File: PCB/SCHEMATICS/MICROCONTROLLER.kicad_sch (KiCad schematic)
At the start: 29 parts, among them IC1 CP2102-GMR, U6 C6482, U7 C6482

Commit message: updated path for footprints
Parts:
- C6: footprint 0ohm:RESC1005X40N -> footprint:RESC1005X40N
- R25, R27: footprint 2.2k:RESC1005X40N -> footprint:RESC1005X40N
- TP22, TP23, TP24, TP25, TP26, TP27, TP32, TP33, TP34, TP35: footprint TestPoint:TestPoint_Bridge_Pitch2.0mm_Drill0.7mm -> TestPoint:TestPoint_Pad_D2.0mm
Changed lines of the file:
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@@
       (effects (font (size 1.27 1.27)))
     )
-    (property "Footprint" "0ohm:RESC1005X40N" (at 127.635 127.635 0)
+    (property "Footprint" "footprint:RESC1005X40N" (at 127.635 127.635 0)
       (effects (font (size 1.27 1.27)) hide)
     )
@@
       (effects (font (size 1.27 1.27)))
     )
-    (property "Footprint" "0ohm:RESC1005X40N" (at 203.2 53.34 0)
+    (property "Footprint" "footprint:RESC1005X40N" (at 203.2 53.34 0)
       (effects (font (size 1.27 1.27)) hide)
     )
@@
       (effects (font (size 1.27 1.27)) (justify right))
     )
-    (property "Footprint" "0ohm:RESC1005X40N" (at 41.91 95.504 0)
+    (property "Footprint" "footprint:RESC1005X40N" (at 41.91 95.504 0)
       (effects (font (size 1.27 1.27)) hide)
     )
@@
       (effects (font (size 1.27 1.27)) (justify left))
     )
-    (property "Footprint" "TestPoint:TestPoint_Bridge_Pitch2.0mm_Drill0.7mm" (at 158.75 39.37 0)
+    (property "Footprint" "TestPoint:TestPoint_Pad_D2.0mm" (at 158.75 39.37 0)
       (effects (font (size 1.27 1.27)) hide)
     )
@@
       (effects (font (size 1.27 1.27)))
     )
-    (property "Footprint" "0ohm:RESC1005X40N" (at 76.2 124.46 0)
+    (property "Footprint" "footprint:RESC1005X40N" (at 76.2 124.46 0)
       (effects (font (size 1.27 1.27)) hide)
     )
@@
       (effects (font (size 1.27 1.27)))
     )
-    (property "Footprint" "2.2k:RESC1005X40N" (at 185.42 53.34 0)
+    (property "Footprint" "footprint:RESC1005X40N" (at 185.42 53.34 0)
       (effects (font (size 1.27 1.27)) hide)
     )
@@
       (effects (font (size 1.27 1.27)))
     )
-    (property "Footprint" "0ohm:RESC1005X40N" (at 127.635 107.315 0)
+    (property "Footprint" "footprint:RESC1005X40N" (at 127.635 107.315 0)
       (effects (font (size 1.27 1.27)) hide)
     )
@@
       (effects (font (size 1.27 1.27)))
     )
-    (property "Footprint" "0ohm:RESC1005X40N" (at 76.2 121.92 0)
+    (property "Footprint" "footprint:RESC1005X40N" (at 76.2 121.92 0)
       (effects (font (size 1.27 1.27)) hide)
     )
@@
       (effects (font (size 1.27 1.27)) (justify left))
     )
-    (property "Footprint" "TestPoint:TestPoint_Bridge_Pitch2.0mm_Drill0.7mm" (at 140.97 39.37 0)
+    (property "Footprint" "TestPoint:TestPoint_Pad_D2.0mm" (at 140.97 39.37 0)
       (effects (font (size 1.27 1.27)) hide)
     )
@@
       (effects (font (size 1.27 1.27)) (justify left))
     )
-    (property "Footprint" "TestPoint:TestPoint_Bridge_Pitch2.0mm_Drill0.7mm" (at 52.07 168.91 0)
+    (property "Footprint" "TestPoint:TestPoint_Pad_D2.0mm" (at 52.07 168.91 0)
       (effects (font (size 1.27 1.27)) hide)
     )
@@
       (effects (font (size 1.27 1.27)))
     )
-    (property "Footprint" "2.2k:RESC1005X40N" (at 185.42 50.8 0)
+    (property "Footprint" "footprint:RESC1005X40N" (at 185.42 50.8 0)
       (effects (font (size 1.27 1.27)) hide)
     )
@@
       (effects (font (size 1.27 1.27)))
     )
-    (property "Footprint" "0ohm:RESC1005X40N" (at 203.2 50.8 0)
+    (property "Footprint" "footprint:RESC1005X40N" (at 203.2 50.8 0)
       (effects (font (size 1.27 1.27)) hide)
     )
@@
       (effects (font (size 1.27 1.27)) (justify left))
     )
-    (property "Footprint" "TestPoint:TestPoint_Bridge_Pitch2.0mm_Drill0.7mm" (at 52.07 171.45 0)
+    (property "Footprint" "TestPoint:TestPoint_Pad_D2.0mm" (at 52.07 171.45 0)
       (effects (font (size 1.27 1.27)) hide)
     )
@@
       (effects (font (size 1.27 1.27)) (justify left))
     )
-    (property "Footprint" "TestPoint:TestPoint_Bridge_Pitch2.0mm_Drill0.7mm" (at 175.26 39.37 0)
+    (property "Footprint" "TestPoint:TestPoint_Pad_D2.0mm" (at 175.26 39.37 0)
       (effects (font (size 1.27 1.27)) hide)
     )
@@
       (effects (font (size 1.27 1.27)) (justify left))
     )
-    (property "Footprint" "TestPoint:TestPoint_Bridge_Pitch2.0mm_Drill0.7mm" (at 52.07 173.99 0)
+    (property "Footprint" "TestPoint:TestPoint_Pad_D2.0mm" (at 52.07 173.99 0)
       (effects (font (size 1.27 1.27)) hide)
     )
@@
       (effects (font (size 1.27 1.27)) (justify left))
     )
-    (property "Footprint" "TestPoint:TestPoint_Bridge_Pitch2.0mm_Drill0.7mm" (at 46.99 158.75 0)
+    (property "Footprint" "TestPoint:TestPoint_Pad_D2.0mm" (at 46.99 158.75 0)
       (effects (font (size 1.27 1.27)) hide)
     )
@@
       (effects (font (size 1.27 1.27)))
     )
-    (property "Footprint" "0ohm:RESC1005X40N" (at 127.635 117.475 0)
+    (property "Footprint" "footprint:RESC1005X40N" (at 127.635 117.475 0)
       (effects (font (size 1.27 1.27)) hide)
     )
@@
       (effects (font (size 1.27 1.27)) (justify left))
     )
-    (property "Footprint" "TestPoint:TestPoint_Bridge_Pitch2.0mm_Drill0.7mm" (at 68.58 107.95 0)
+    (property "Footprint" "TestPoint:TestPoint_Pad_D2.0mm" (at 68.58 107.95 0)
       (effects (font (size 1.27 1.27)) hide)
     )
@@
       (effects (font (size 1.27 1.27)) (justify left))
     )
-    (property "Footprint" "TestPoint:TestPoint_Bridge_Pitch2.0mm_Drill0.7mm" (at 76.2 107.95 0)
+    (property "Footprint" "TestPoint:TestPoint_Pad_D2.0mm" (at 76.2 107.95 0)
       (effects (font (size 1.27 1.27)) hide)
     )
@@
       (effects (font (size 1.27 1.27)) (justify left))
     )
-    (property "Footprint" "TestPoint:TestPoint_Bridge_Pitch2.0mm_Drill0.7mm" (at 59.69 96.52 0)
-      (effects (font (size 1.27 1.27)) hide)
-    )
+    (property "Footprint" "TestPoint:TestPoint_Pad_D2.0mm" (at 59.69 96.52 0)
+      (effects (font (size 1.27 1.27)) hide)
+    )

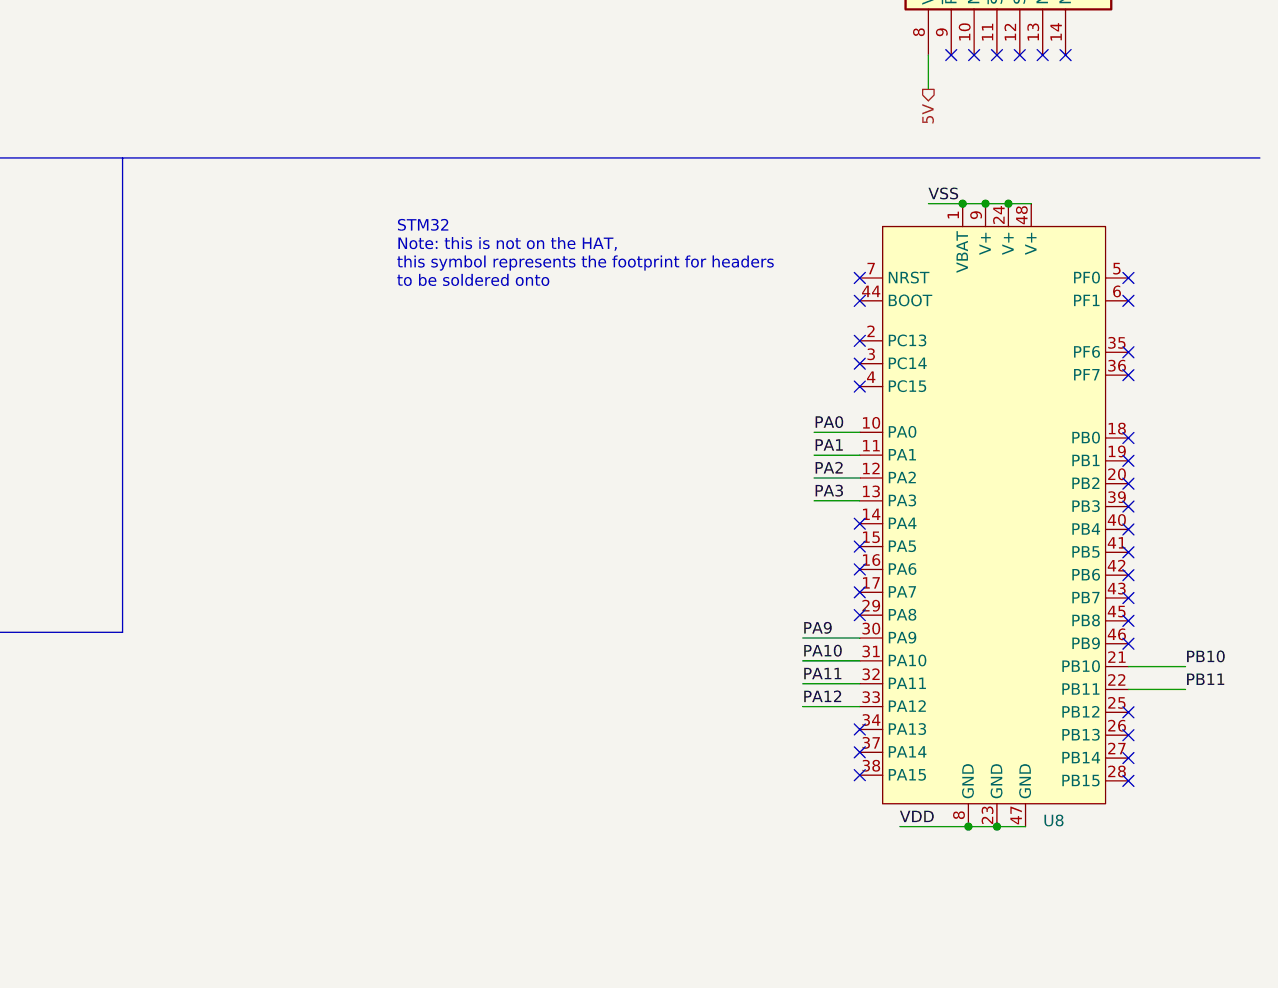
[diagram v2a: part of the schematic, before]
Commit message: Added parallel headers and edge cuts
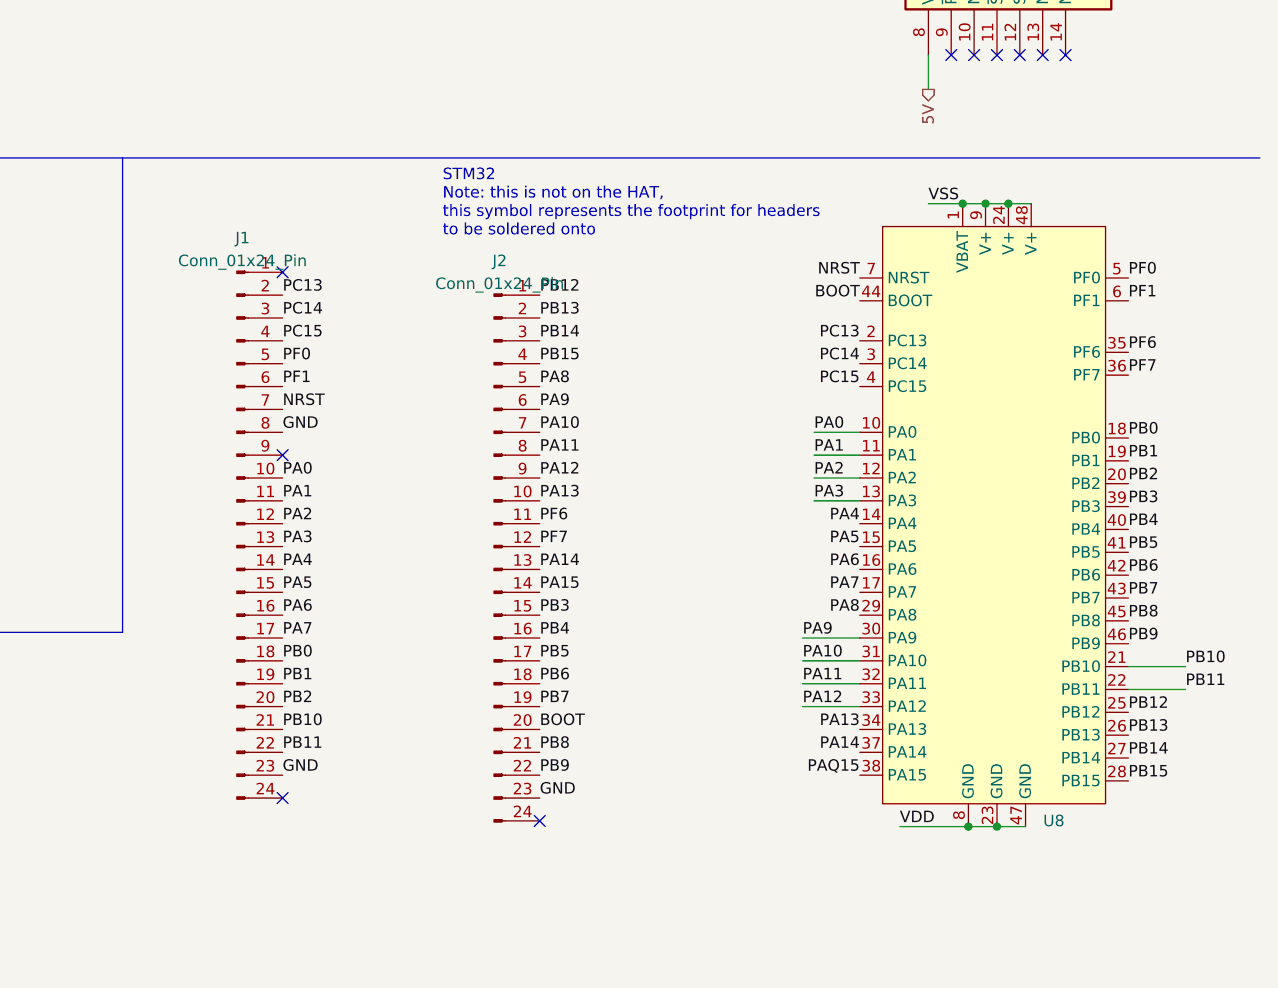
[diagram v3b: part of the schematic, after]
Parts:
- added J1, J2: Conn_01x24_Pin, Connector_PinSocket_2.54mm:PinSocket_1x24_P2.54mm_Vertical, symbol Connector:Conn_01x24_Pin
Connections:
- net Battery_sensor_output: now also J1.13 (Pin_13)
- net GND: now also J1.23 (Pin_23), J1.8 (Pin_8), J2.23 (Pin_23)
- net Light_sensor_SCL: now also J1.21 (Pin_21)
- net Light_sensor_SDA: now also J1.22 (Pin_22)
- net PA0: now also J1.10 (Pin_10)
- net PA1: now also J1.11 (Pin_11)
- net PA10: now also J2.7 (Pin_7)
- net PA11: now also J2.8 (Pin_8)
- net PA12: now also J2.9 (Pin_9)
- net PA2: now also J1.12 (Pin_12)
- net PA9: now also J2.6 (Pin_6)
- net PA4: now reaches U8.14 (PA4)
- net PA4: now also J1.14 (Pin_14)
- net PA5: now reaches U8.15 (PA5)
- net PA5: now also J1.15 (Pin_15)
- net PA6: now reaches U8.16 (PA6)
- net PA6: now also J1.16 (Pin_16)
- net PA7: now reaches U8.17 (PA7)
- net PA7: now also J1.17 (Pin_17)
- net PB0: now reaches U8.18 (PB0)
- net PB0: now also J1.18 (Pin_18)
- net PB1: now reaches U8.19 (PB1)
- net PB1: now also J1.19 (Pin_19)
- net PC13: now reaches U8.2 (PC13)
- net PC13: now also J1.2 (Pin_2)
- net PB2: now reaches U8.20 (PB2)
- net PB2: now also J1.20 (Pin_20)
- net PB12: now reaches U8.25 (PB12)
- net PB12: now also J2.1 (Pin_1)
- net PB13: now reaches U8.26 (PB13)
- net PB13: now also J2.2 (Pin_2)
- net PB14: now reaches U8.27 (PB14)
- net PB14: now also J2.3 (Pin_3)
- net PB15: now reaches U8.28 (PB15)
- net PB15: now also J2.4 (Pin_4)
- net PA8: now reaches U8.29 (PA8)
- net PA8: now also J2.5 (Pin_5)
- net PC14: now reaches U8.3 (PC14)
- net PC14: now also J1.3 (Pin_3)
- net PA13: now reaches U8.34 (PA13)
- net PA13: now also J2.10 (Pin_10)
- net PF6: now reaches U8.35 (PF6)
- net PF6: now also J2.11 (Pin_11)
- net PF7: now reaches U8.36 (PF7)
- net PF7: now also J2.12 (Pin_12)
- net PA14: now reaches U8.37 (PA14)
- net PA14: now also J2.13 (Pin_13)
- net PAQ15: now reaches U8.38 (PA15)
- net PB3: now reaches U8.39 (PB3)
- net PB3: now also J2.15 (Pin_15)
- net PC15: now reaches U8.4 (PC15)
- net PC15: now also J1.4 (Pin_4)
- net PB4: now reaches U8.40 (PB4)
- net PB4: now also J2.16 (Pin_16)
- net PB5: now reaches U8.41 (PB5)
- net PB5: now also J2.17 (Pin_17)
- net PB6: now reaches U8.42 (PB6)
- net PB6: now also J2.18 (Pin_18)
- net PB7: now reaches U8.43 (PB7)
- net PB7: now also J2.19 (Pin_19)
- net BOOT: now reaches U8.44 (BOOT)
- net BOOT: now also J2.20 (Pin_20)
- net PB8: now reaches U8.45 (PB8)
- net PB8: now also J2.21 (Pin_21)
- net PB9: now reaches U8.46 (PB9)
- net PB9: now also J2.22 (Pin_22)
- net PF0: now reaches U8.5 (PF0)
- net PF0: now also J1.5 (Pin_5)
- net PF1: now reaches U8.6 (PF1)
- net PF1: now also J1.6 (Pin_6)
- net NRST: now reaches U8.7 (NRST)
- net NRST: now also J1.7 (Pin_7)
- new net PA15: J2.14 (Pin_14)
- no-connect marks 53 -> 26

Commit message: Updated pcb
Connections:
- net PAQ15 is gone; now on net PA15: U8.38 (PA15)
- net PB9 is gone; now on net Battery_sensor_output: J2.22 (Pin_22), U8.46 (PB9)
- net Battery_sensor_output: no longer J1.13 (Pin_13), U8.13 (PA3)
- new net PA3: J1.13 (Pin_13), U8.13 (PA3)
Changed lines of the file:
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@@
     (effects (font (size 1.27 1.27)) (justify left bottom))
   )
-  (label "PA3" (at 49.53 33.02 0) (fields_autoplaced)
+  (label "PB9" (at 49.53 33.02 0) (fields_autoplaced)
     (effects (font (size 1.27 1.27)) (justify left bottom))
   )
@@
     (effects (font (size 1.27 1.27)) (justify left bottom))
   )
-  (label "PAQ15" (at 240.03 157.48 180) (fields_autoplaced)
+  (label "PA15" (at 240.03 157.48 180) (fields_autoplaced)
     (effects (font (size 1.27 1.27)) (justify right bottom))
   )

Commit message: Labeled modules
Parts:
- J1, J2: now not fitted; now left out of the parts list
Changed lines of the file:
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@@
   )
   (symbol (lib_id "Connector:Conn_01x24_Pin") (at 199.39 132.08 0) (unit 1)
-    (in_bom yes) (on_board yes) (dnp no) (fields_autoplaced)
+    (in_bom no) (on_board yes) (dnp yes) (fields_autoplaced)
     (property "Reference" "J2" (at 200.025 100.33 0)
       (effects (font (size 1.27 1.27)))
@@
   )
   (symbol (lib_id "Connector:Conn_01x24_Pin") (at 170.815 129.54 0) (unit 1)
-    (in_bom yes) (on_board yes) (dnp no) (fields_autoplaced)
+    (in_bom no) (on_board yes) (dnp yes) (fields_autoplaced)
     (property "Reference" "J1" (at 171.45 97.79 0)
       (effects (font (size 1.27 1.27)))

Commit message: Added final docs
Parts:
- removed R25, R27: 2.2k, footprint:RESC1005X40N, symbol Device:R_Small_US
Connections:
- net at C6.1: now also MicroXNJ1.3 (D+), TP24.1
- net at MicroXNJ1.2 (D-), TP23.1: now also C6.1
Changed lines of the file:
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@@
-    (stroke (width 0) (type default))
-  )
-  (wire (pts (xy 187.96 53.34) (xy 200.66 53.34))
     (stroke (width 0) (type default))
   )
@@
     (stroke (width 0) (type default))
   )
-  (wire (pts (xy 187.96 50.8) (xy 200.66 50.8))
-    (stroke (width 0) (type default))
-  )
   (wire (pts (xy 153.67 39.37) (xy 153.67 50.8))
     (stroke (width 0) (type default))
@@
     (stroke (width 0) (type default))
   )
-  (wire (pts (xy 153.67 50.8) (xy 182.88 50.8))
+  (wire (pts (xy 153.67 50.8) (xy 200.66 50.8))
     (stroke (width 0) (type default))
   )
@@
     (stroke (width 0) (type default))
   )
-  (wire (pts (xy 170.18 53.34) (xy 182.88 53.34))
+  (wire (pts (xy 170.18 53.34) (xy 200.66 53.34))
     (stroke (width 0) (type default))
   )
@@
         (path "/c9ca3a5c-30cb-4dce-b611-3270b9f3284b/f1cf3ff5-1ffc-45ee-bf83-2ece91c9ccf0"
           (reference "#PWR03") (unit 1)
-        )
-      )
-    )
-  )
-  (symbol (lib_id "Device:R_Small_US") (at 185.42 53.34 90) (unit 1)
-    (in_bom yes) (on_board yes) (dnp no)
-    (property "Reference" "R27" (at 185.42 55.88 90)
-      (effects (font (size 1.27 1.27)))
-    )
-    (property "Value" "2.2k" (at 185.42 58.42 90)
-      (effects (font (size 1.27 1.27)))
-    )
-    (property "Footprint" "footprint:RESC1005X40N" (at 185.42 53.34 0)
-      (effects (font (size 1.27 1.27)) hide)
-    )
-    (property "Datasheet" "~" (at 185.42 53.34 0)
-      (effects (font (size 1.27 1.27)) hide)
-    )
-    (property "PART " "    C17520" (at 185.42 53.34 0)
-      (effects (font (size 1.27 1.27)) hide)
-    )
-    (property "Unit Price" "0.0017" (at 185.42 53.34 0)
-      (effects (font (size 1.27 1.27)) hide)
-    )
-    (pin "1")
-    (pin "2")
-    (instances
-      (project "SCHEMATICS"
-        (path "/c9ca3a5c-30cb-4dce-b611-3270b9f3284b/f1cf3ff5-1ffc-45ee-bf83-2ece91c9ccf0"
-          (reference "R27") (unit 1)
         )
       )
@@
         )
       )
-    )
-  )
-  (symbol (lib_id "Device:R_Small_US") (at 185.42 50.8 90) (unit 1)
-    (in_bom yes) (on_board yes) (dnp no)
-    (property "Reference" "R25" (at 185.42 45.72 90)
-      (effects (font (size 1.27 1.27)))
-    )
-    (property "Value" "2.2k" (at 185.42 48.26 90)
-      (effects (font (size 1.27 1.27)))
-    )
-    (property "Footprint" "footprint:RESC1005X40N" (at 185.42 50.8 0)
-      (effects (font (size 1.27 1.27)) hide)
-    )
-    (property "Datasheet" "~" (at 185.42 50.8 0)
-      (effects (font (size 1.27 1.27)) hide)
-    )
-    (property "PART " "    C17520" (at 185.42 50.8 0)
-      (effects (font (size 1.27 1.27)) hide)
-    )
-    (property "Unit Price" "0.0017" (at 185.42 50.8 0)
-      (effects (font (size 1.27 1.27)) hide)
-    )
-    (pin "1")
-    (pin "2")
-    (instances
-      (project "SCHEMATICS"
-        (path "/c9ca3a5c-30cb-4dce-b611-3270b9f3284b/f1cf3ff5-1ffc-45ee-bf83-2ece91c9ccf0"
-          (reference "R25") (unit 1)
-        )
-      )

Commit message: Justins reccomendations
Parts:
- removed C6 (x3): 0, footprint:RESC1005X40N, symbol Device:R_Small_US
- removed TP32, TP33, TP34, TP35: TestPoint, TestPoint:TestPoint_Pad_D2.0mm, symbol Connector:TestPoint
- removed U7: C6482, footprint:SOIC-8_L4.9-W3.9-P1.27-LS6.0-BL, symbol Memory_EEPROM:24LC08
- added R19 (x3): 1k, footprint:R0402, symbol Device:R_Small_US
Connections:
- net PA0: now also R19.2
- net PA1: now also R19.2
- net PA2: now also R19.2
- net at D8.2 (A): now also R19.1
- net at D6.2 (A): now also R19.1
- net at D7.2 (A): now also R19.1
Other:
- note removed: "Spare EEPROM"
